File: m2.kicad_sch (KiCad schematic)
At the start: 61 parts, among them J13 Bus_M.2_1-2199230-6, J14 Bus_M.2_2199230-2, Y3 Oscillator_32.768kHz_ECS_2520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

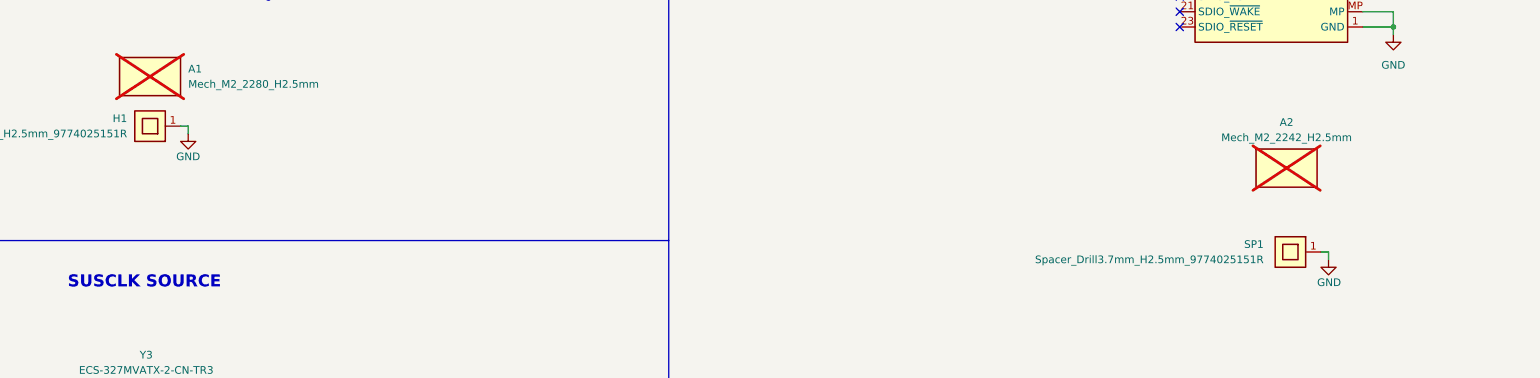
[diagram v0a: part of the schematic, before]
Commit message: [#82847] Prepare current state of schematic to merge with mockup
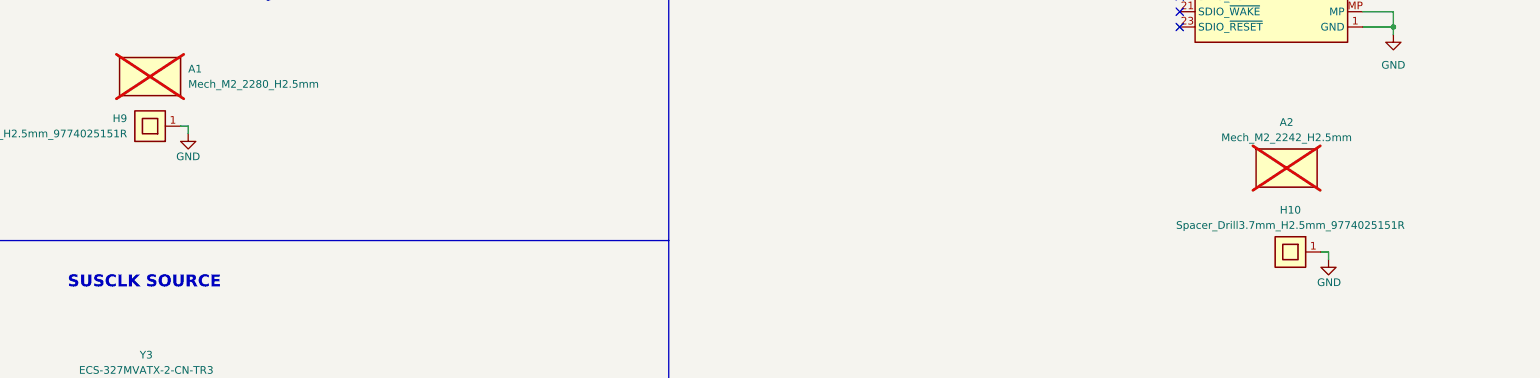
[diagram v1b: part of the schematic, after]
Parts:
- renumbered SP1 to H10, H1 to H9
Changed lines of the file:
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@@
 		(on_board yes)
 		(dnp no)
-		(property "Reference" "#PWR0379"
+		(property "Reference" "#PWR0381"
 			(at 327.66 101.6 0)
 			(effects
@@
 			(project "jetson-agx-thor-baseboard"
 				(path "/f569b0be-0afd-48b7-93ee-28582a4c645c/456a2f48-4934-4d0e-aaf0-f39b01ccc0c1"
-					(reference "#PWR0379")
+					(reference "#PWR0381")
 					(unit 1)
 				)
@@
 		(on_board yes)
 		(dnp no)
-		(property "Reference" "#PWR0367"
+		(property "Reference" "#PWR0369"
 			(at 147.32 111.76 0)
 			(effects
@@
 			(project "jetson-agx-thor-baseboard"
 				(path "/f569b0be-0afd-48b7-93ee-28582a4c645c/456a2f48-4934-4d0e-aaf0-f39b01ccc0c1"
-					(reference "#PWR0367")
+					(reference "#PWR0369")
 					(unit 1)
 				)
@@
 		(on_board yes)
 		(dnp no)
-		(property "Reference" "#PWR0377"
+		(property "Reference" "#PWR0379"
 			(at 318.77 101.6 0)
 			(effects
@@
 			(project "jetson-agx-thor-baseboard"
 				(path "/f569b0be-0afd-48b7-93ee-28582a4c645c/456a2f48-4934-4d0e-aaf0-f39b01ccc0c1"
-					(reference "#PWR0377")
+					(reference "#PWR0379")
 					(unit 1)
 				)
@@
 		(on_board yes)
 		(dnp no)
-		(property "Reference" "#PWR0365"
+		(property "Reference" "#PWR0367"
 			(at 132.08 187.96 0)
 			(effects
@@
 			(project "jetson-agx-thor-baseboard"
 				(path "/f569b0be-0afd-48b7-93ee-28582a4c645c/456a2f48-4934-4d0e-aaf0-f39b01ccc0c1"
-					(reference "#PWR0365")
+					(reference "#PWR0367")
 					(unit 1)
 				)
@@
 		(on_board yes)
 		(dnp no)
-		(property "Reference" "#PWR0363"
+		(property "Reference" "#PWR0365"
 			(at 106.68 218.44 0)
 			(effects
@@
 			(project "jetson-agx-thor-baseboard"
 				(path "/f569b0be-0afd-48b7-93ee-28582a4c645c/456a2f48-4934-4d0e-aaf0-f39b01ccc0c1"
-					(reference "#PWR0363")
+					(reference "#PWR0365")
 					(unit 1)
 				)
@@
 		(dnp no)
 		(fields_autoplaced yes)
-		(property "Reference" "SP1"
-			(at 276.86 234.315 0)
+		(property "Reference" "H10"
+			(at 281.305 228.6 0)
 			(effects
 				(font
@@
 					(thickness 0.15)
 				)
-				(justify left)
 			)
 		)
 		(property "Value" "Spacer_Drill3.7mm_H2.5mm_9774025151R"
-			(at 276.86 236.855 0)
+			(at 281.305 231.14 0)
 			(effects
 				(font
@@
 					(thickness 0.15)
 				)
-				(justify left)
 			)
 		)
@@
 			(project "jetson-agx-thor-baseboard"
 				(path "/f569b0be-0afd-48b7-93ee-28582a4c645c/456a2f48-4934-4d0e-aaf0-f39b01ccc0c1"
-					(reference "SP1")
+					(reference "H10")
 					(unit 1)
 				)
@@
 		(on_board yes)
 		(dnp no)
-		(property "Reference" "H1"
+		(property "Reference" "H9"
 			(at 87.63 213.36 0)
 			(effects
@@
 			(project "jetson-agx-thor-baseboard"
 				(path "/f569b0be-0afd-48b7-93ee-28582a4c645c/456a2f48-4934-4d0e-aaf0-f39b01ccc0c1"
-					(reference "H1")
+					(reference "H9")
 					(unit 1)
 				)
@@
 		(on_board yes)
 		(dnp no)
-		(property "Reference" "#PWR0376"
+		(property "Reference" "#PWR0378"
 			(at 314.96 168.91 0)
 			(effects
@@
 			(project "jetson-agx-thor-baseboard"
 				(path "/f569b0be-0afd-48b7-93ee-28582a4c645c/456a2f48-4934-4d0e-aaf0-f39b01ccc0c1"
-					(reference "#PWR0376")
+					(reference "#PWR0378")
 					(unit 1)
 				)
@@
 		(dnp no)
 		(fields_autoplaced yes)
-		(property "Reference" "#PWR0373"
+		(property "Reference" "#PWR0375"
 			(at 298.45 205.74 0)
 			(effects
@@
 			(project "jetson-agx-thor-baseboard"
 				(path "/f569b0be-0afd-48b7-93ee-28582a4c645c/456a2f48-4934-4d0e-aaf0-f39b01ccc0c1"
-					(reference "#PWR0373")
+					(reference "#PWR0375")
 					(unit 1)
 				)
@@
 		(on_board yes)
 		(dnp no)
-		(property "Reference" "#PWR0374"
+		(property "Reference" "#PWR0376"
 			(at 300.99 101.6 0)
 			(effects
@@
 			(project "jetson-agx-thor-baseboard"
 				(path "/f569b0be-0afd-48b7-93ee-28582a4c645c/456a2f48-4934-4d0e-aaf0-f39b01ccc0c1"
-					(reference "#PWR0374")
+					(reference "#PWR0376")
 					(unit 1)
 				)
@@
 		(on_board yes)
 		(dnp no)
-		(property "Reference" "#PWR0360"
+		(property "Reference" "#PWR0362"
 			(at 73.66 276.86 0)
 			(effects
@@
 			(project "jetson-agx-thor-baseboard"
 				(path "/f569b0be-0afd-48b7-93ee-28582a4c645c/456a2f48-4934-4d0e-aaf0-f39b01ccc0c1"
-					(reference "#PWR0360")
+					(reference "#PWR0362")
 					(unit 1)
 				)
@@
 		(dnp no)
 		(fields_autoplaced yes)
-		(property "Reference" "#PWR0371"
+		(property "Reference" "#PWR0373"
 			(at 246.38 88.9 0)
 			(effects
@@
 			(project "jetson-agx-thor-baseboard"
 				(path "/f569b0be-0afd-48b7-93ee-28582a4c645c/456a2f48-4934-4d0e-aaf0-f39b01ccc0c1"
-					(reference "#PWR0371")
+					(reference "#PWR0373")
 					(unit 1)
 				)
@@
 		(on_board yes)
 		(dnp no)
-		(property "Reference" "#PWR0361"
+		(property "Reference" "#PWR0363"
 			(at 80.01 276.86 0)
 			(effects
@@
 			(project "jetson-agx-thor-baseboard"
 				(path "/f569b0be-0afd-48b7-93ee-28582a4c645c/456a2f48-4934-4d0e-aaf0-f39b01ccc0c1"
-					(reference "#PWR0361")
+					(reference "#PWR0363")
 					(unit 1)
 				)
@@
 		(on_board yes)
 		(dnp no)
-		(property "Reference" "#PWR0380"
+		(property "Reference" "#PWR0382"
 			(at 327.66 168.91 0)
 			(effects
@@
 			(project "jetson-agx-thor-baseboard"
 				(path "/f569b0be-0afd-48b7-93ee-28582a4c645c/456a2f48-4934-4d0e-aaf0-f39b01ccc0c1"
-					(reference "#PWR0380")
+					(reference "#PWR0382")
 					(unit 1)
 				)
@@
 		(on_board yes)
 		(dnp no)
-		(property "Reference" "#PWR0364"
+		(property "Reference" "#PWR0366"
 			(at 132.08 144.78 0)
 			(effects
@@
 			(project "jetson-agx-thor-baseboard"
 				(path "/f569b0be-0afd-48b7-93ee-28582a4c645c/456a2f48-4934-4d0e-aaf0-f39b01ccc0c1"
-					(reference "#PWR0364")
+					(reference "#PWR0366")
 					(unit 1)
 				)
@@
 		(on_board yes)
 		(dnp no)
-		(property "Reference" "#PWR0366"
+		(property "Reference" "#PWR0368"
 			(at 137.16 111.76 0)
 			(effects
@@
 			(project "jetson-agx-thor-baseboard"
 				(path "/f569b0be-0afd-48b7-93ee-28582a4c645c/456a2f48-4934-4d0e-aaf0-f39b01ccc0c1"
-					(reference "#PWR0366")
+					(reference "#PWR0368")
 					(unit 1)
 				)
@@
 		(on_board yes)
 		(dnp no)
-		(property "Reference" "#PWR0359"
+		(property "Reference" "#PWR0361"
 			(at 73.66 265.43 0)
 			(effects
@@
 			(project "jetson-agx-thor-baseboard"
 				(path "/f569b0be-0afd-48b7-93ee-28582a4c645c/456a2f48-4934-4d0e-aaf0-f39b01ccc0c1"
-					(reference "#PWR0359")
+					(reference "#PWR0361")
 					(unit 1)
 				)
@@
 		(on_board yes)
 		(dnp no)
-		(property "Reference" "#PWR0368"
+		(property "Reference" "#PWR0370"
 			(at 157.48 111.76 0)
 			(effects
@@
 			(project "jetson-agx-thor-baseboard"
 				(path "/f569b0be-0afd-48b7-93ee-28582a4c645c/456a2f48-4934-4d0e-aaf0-f39b01ccc0c1"
-					(reference "#PWR0368")
+					(reference "#PWR0370")
 					(unit 1)
 				)
@@
 		(on_board yes)
 		(dnp no)
-		(property "Reference" "#PWR0372"
+		(property "Reference" "#PWR0374"
 			(at 287.655 243.205 0)
 			(effects
@@
 			(project "jetson-agx-thor-baseboard"
 				(path "/f569b0be-0afd-48b7-93ee-28582a4c645c/456a2f48-4934-4d0e-aaf0-f39b01ccc0c1"
-					(reference "#PWR0372")
+					(reference "#PWR0374")
 					(unit 1)
 				)
@@
 		(on_board yes)
 		(dnp no)
-		(property "Reference" "#PWR0369"
+		(property "Reference" "#PWR0371"
 			(at 167.64 92.71 0)
 			(effects
@@
 			(project "jetson-agx-thor-baseboard"
 				(path "/f569b0be-0afd-48b7-93ee-28582a4c645c/456a2f48-4934-4d0e-aaf0-f39b01ccc0c1"
-					(reference "#PWR0369")
+					(reference "#PWR0371")
 					(unit 1)
 				)
@@
 		(on_board yes)
 		(dnp no)
-		(property "Reference" "#PWR0381"
+		(property "Reference" "#PWR0383"
 			(at 340.36 137.16 0)
 			(effects
@@
 			(project "jetson-agx-thor-baseboard"
 				(path "/f569b0be-0afd-48b7-93ee-28582a4c645c/456a2f48-4934-4d0e-aaf0-f39b01ccc0c1"
-					(reference "#PWR0381")
+					(reference "#PWR0383")
 					(unit 1)
 				)
@@
 		(on_board yes)
 		(dnp no)
-		(property "Reference" "#PWR0370"
+		(property "Reference" "#PWR0372"
 			(at 167.64 111.76 0)
 			(effects
@@
 			(project "jetson-agx-thor-baseboard"
 				(path "/f569b0be-0afd-48b7-93ee-28582a4c645c/456a2f48-4934-4d0e-aaf0-f39b01ccc0c1"
-					(reference "#PWR0370")
+					(reference "#PWR0372")
 					(unit 1)
 				)
@@
 		(on_board yes)
 		(dnp no)
-		(property "Reference" "#PWR0362"
+		(property "Reference" "#PWR0364"
 			(at 83.82 97.79 0)
 			(effects
@@
 			(project "jetson-agx-thor-baseboard"
 				(path "/f569b0be-0afd-48b7-93ee-28582a4c645c/456a2f48-4934-4d0e-aaf0-f39b01ccc0c1"
-					(reference "#PWR0362")
+					(reference "#PWR0364")
 					(unit 1)
 				)
@@
 		(on_board yes)
 		(dnp no)
-		(property "Reference" "#PWR0378"
+		(property "Reference" "#PWR0380"
 			(at 327.66 87.63 0)
 			(effects
@@
 			(project "jetson-agx-thor-baseboard"
 				(path "/f569b0be-0afd-48b7-93ee-28582a4c645c/456a2f48-4934-4d0e-aaf0-f39b01ccc0c1"
-					(reference "#PWR0378")
+					(reference "#PWR0380")
 					(unit 1)
 				)
@@
 		(on_board yes)
 		(dnp no)
-		(property "Reference" "#PWR0375"
+		(property "Reference" "#PWR0377"
 			(at 309.88 101.6 0)
 			(effects
@@
 			(project "jetson-agx-thor-baseboard"
 				(path "/f569b0be-0afd-48b7-93ee-28582a4c645c/456a2f48-4934-4d0e-aaf0-f39b01ccc0c1"
-					(reference "#PWR0375")
+					(reference "#PWR0377")
 					(unit 1)
 				)

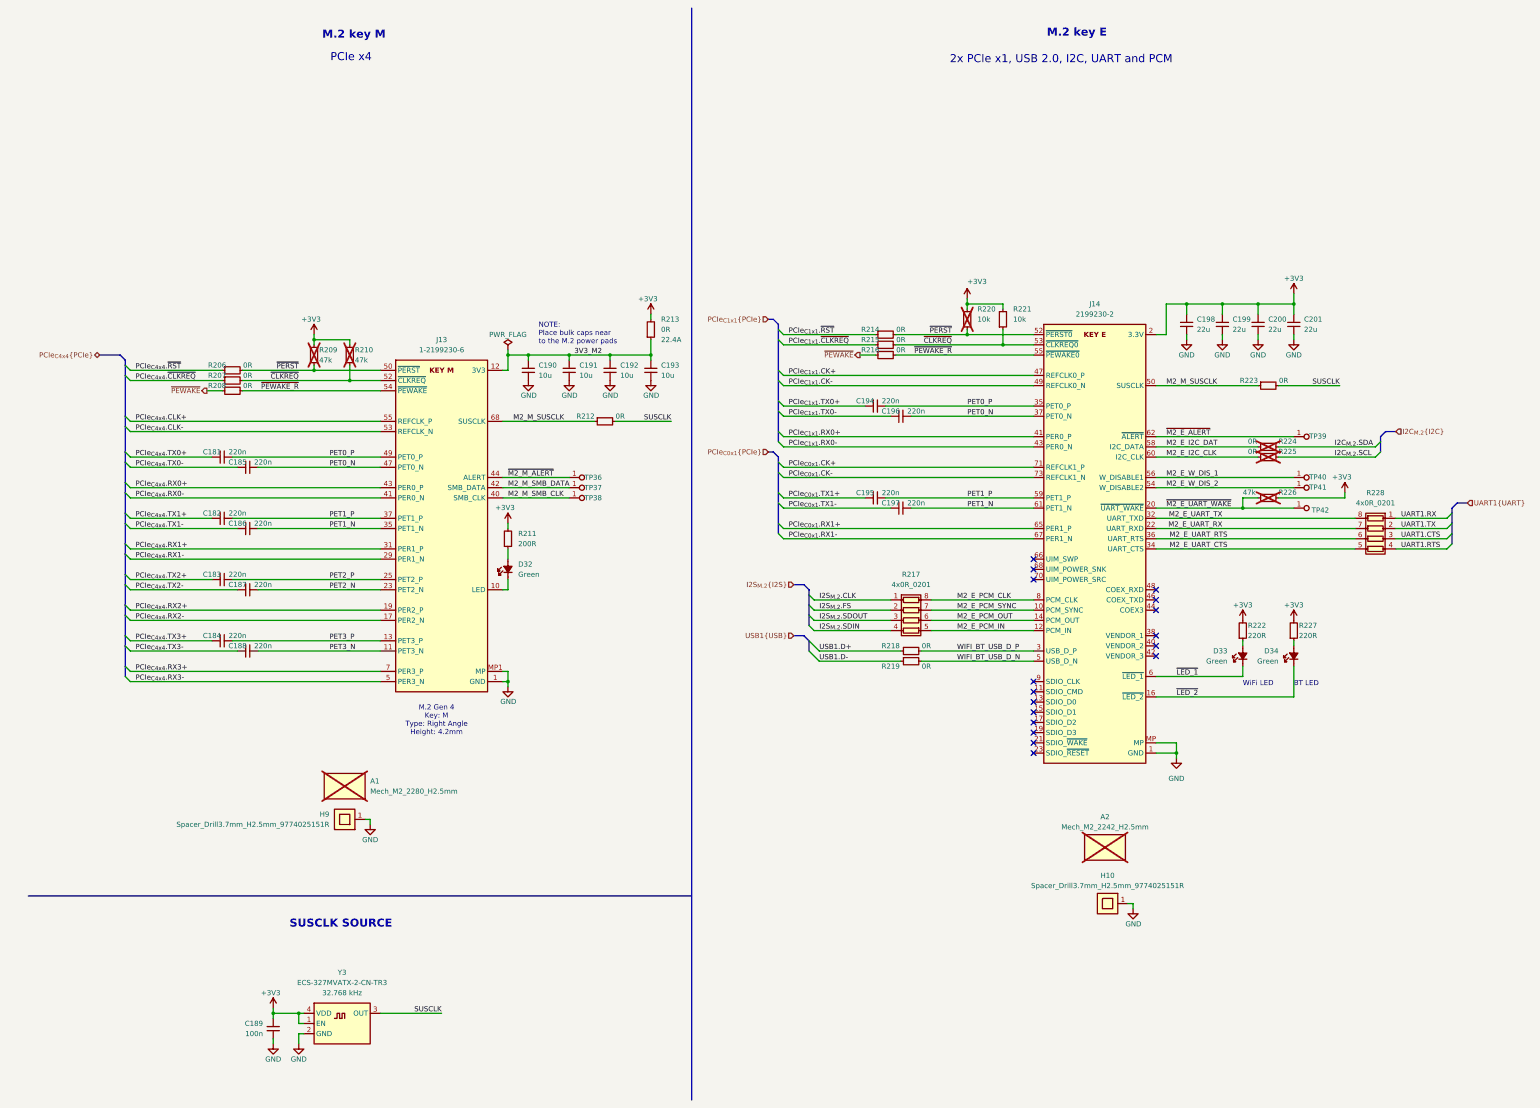
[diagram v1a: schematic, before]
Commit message: [#82837] Standardise sheet sections text size
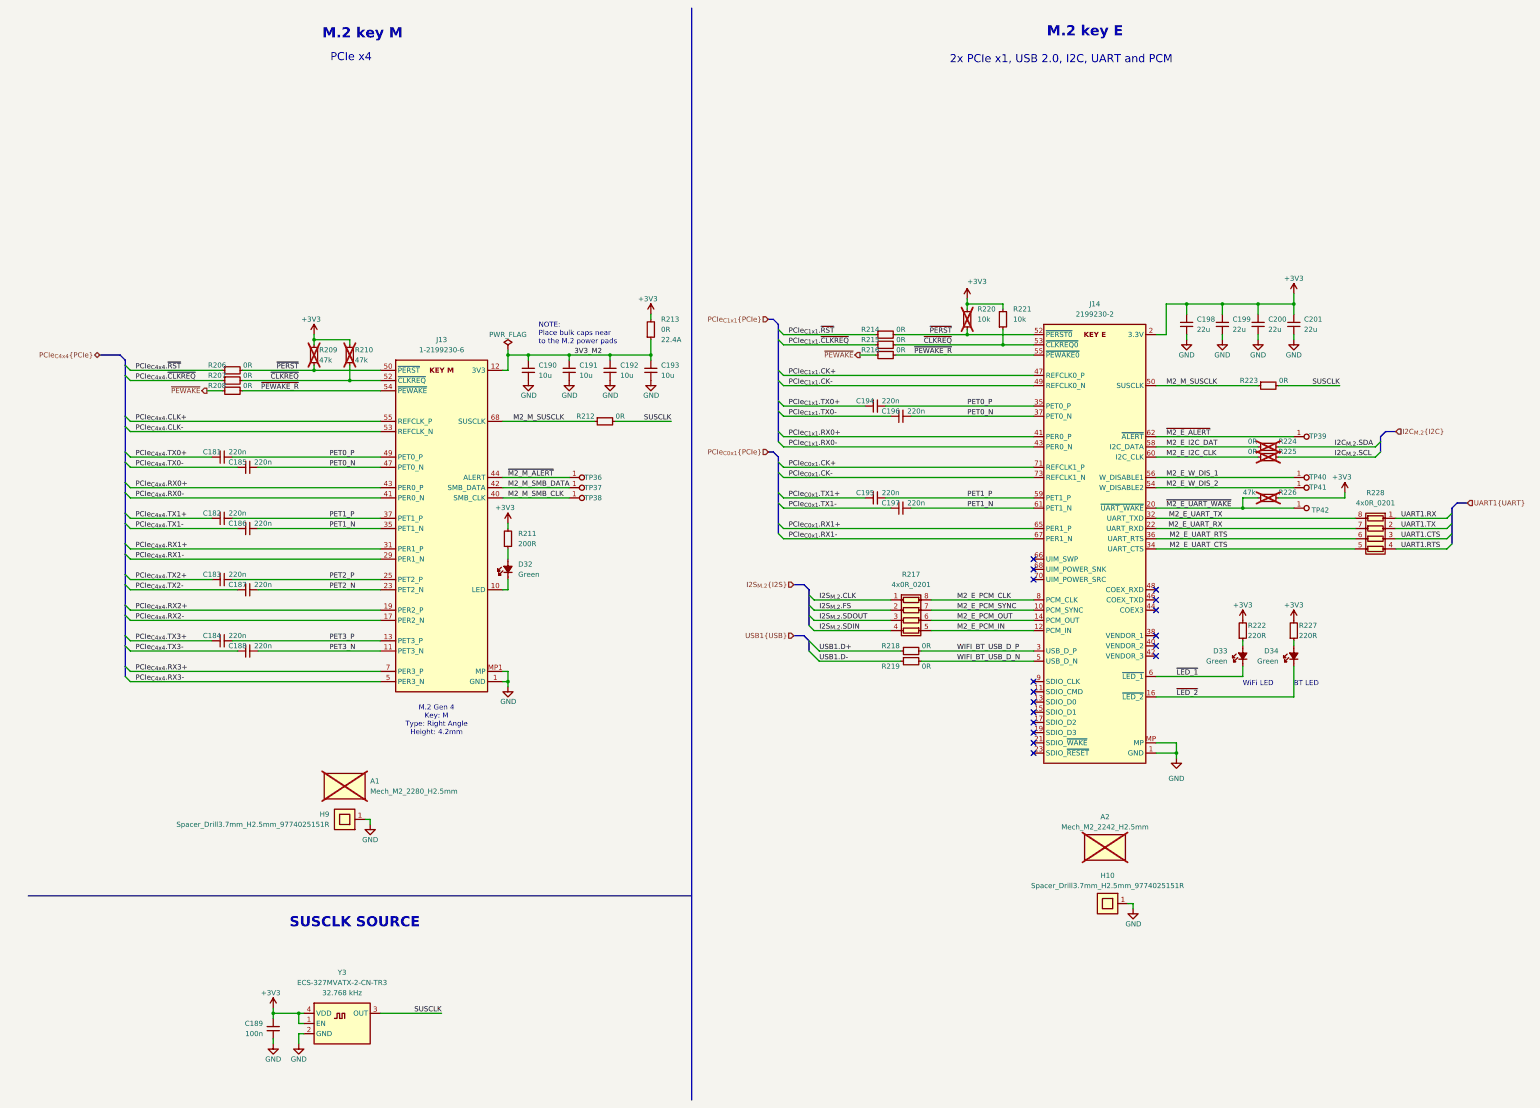
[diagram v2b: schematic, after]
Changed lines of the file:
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@@
 		(effects
 			(font
-				(size 2 2)
+				(size 2.54 2.54)
 				(thickness 0.508)
 				(bold yes)
@@
 		(effects
 			(font
-				(size 2 2)
+				(size 2.54 2.54)
 				(thickness 0.508)
 				(bold yes)
@@
 		(effects
 			(font
-				(size 2 2)
+				(size 2.54 2.54)
 				(thickness 0.508)
 				(bold yes)

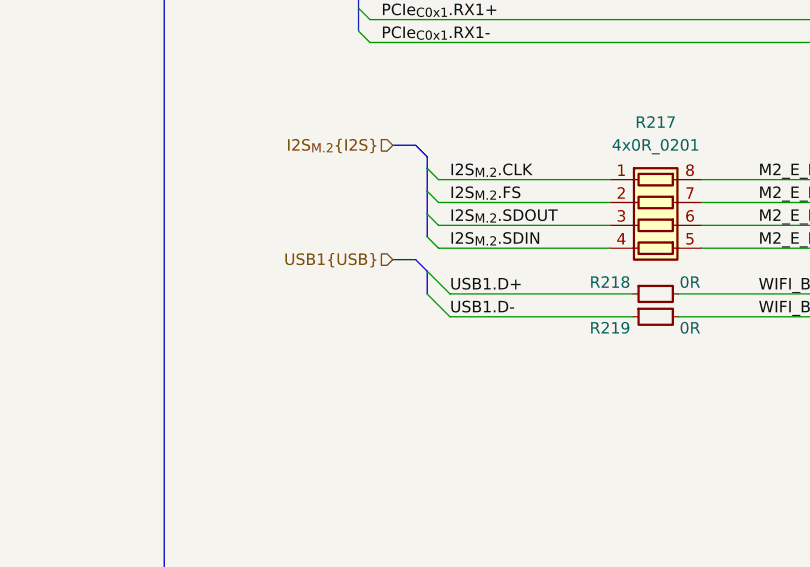
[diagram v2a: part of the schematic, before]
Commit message: [#82837] Wire USB section on root schematic
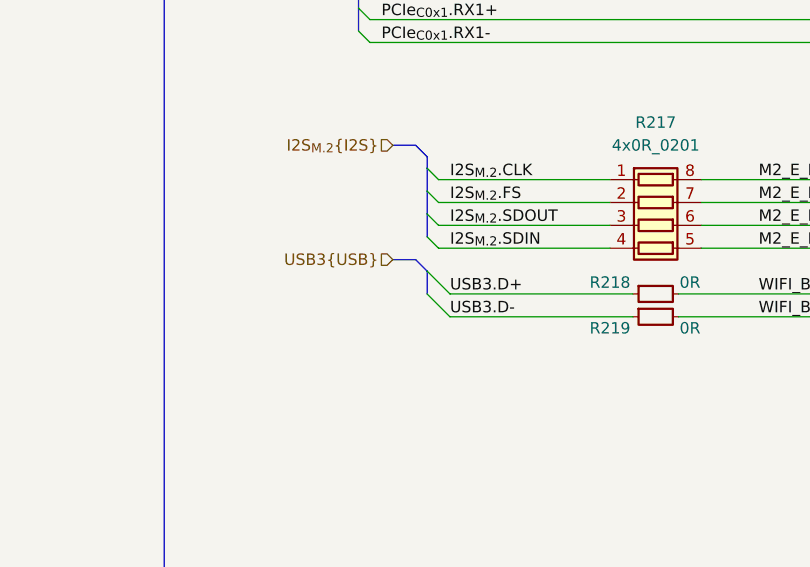
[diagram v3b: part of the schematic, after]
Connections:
- net USB1.D+ renamed USB3.D+
- net USB1.D- renamed USB3.D-
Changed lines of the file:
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@@
 		)
 	)
-	(label "USB1.D-"
+	(label "USB3.D-"
 		(at 209.55 175.26 0)
 		(effects
@@
 		)
 	)
-	(label "USB1.D+"
+	(label "USB3.D+"
 		(at 209.55 172.72 0)
 		(effects
@@
 		)
 	)
-	(hierarchical_label "USB1{USB}"
+	(hierarchical_label "USB3{USB}"
 		(shape input)
 		(at 203.2 168.91 180)
